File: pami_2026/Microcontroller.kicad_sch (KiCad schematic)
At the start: 20 parts, among them SW1 SW_Reed, U1 ESP32-WROOM-E

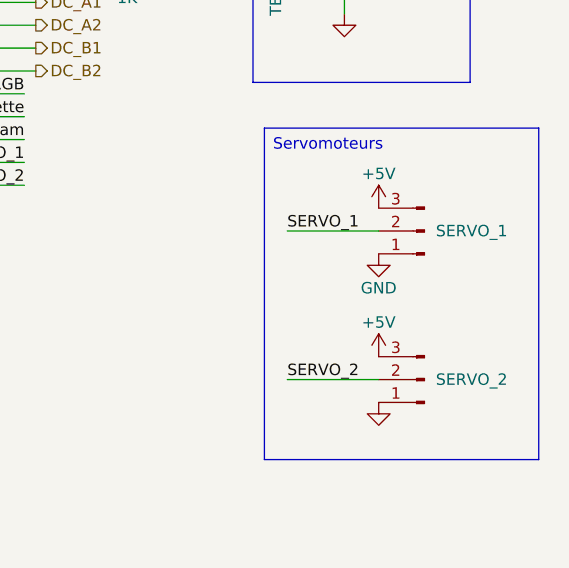
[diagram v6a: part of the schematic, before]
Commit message: Fix servo pinout
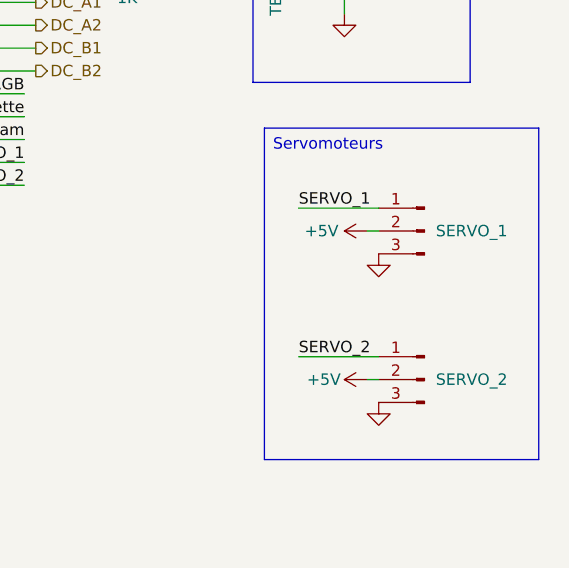
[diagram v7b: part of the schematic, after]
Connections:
- net +5V: now also SERVO_1.2 (Pin_2), SERVO_2.2 (Pin_2); no longer SERVO_1.3 (Pin_3), SERVO_2.3 (Pin_3)
- net GND: now also SERVO_1.3 (Pin_3), SERVO_2.3 (Pin_3); no longer SERVO_1.1 (Pin_1), SERVO_2.1 (Pin_1)
- net SERVO_1: now also SERVO_1.1 (Pin_1); no longer SERVO_1.2 (Pin_2)
- net SERVO_2: now also SERVO_2.1 (Pin_1); no longer SERVO_2.2 (Pin_2)
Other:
- moved on the sheet: SERVO_1, SERVO_2
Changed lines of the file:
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@@
 	(wire
 		(pts
-			(xy 71.12 152.4) (xy 81.28 152.4)
+			(xy 223.52 146.05) (xy 232.41 146.05)
 		)
 		(stroke
@@
 	(wire
 		(pts
-			(xy 97.79 82.55) (xy 97.79 81.28)
+			(xy 71.12 152.4) (xy 81.28 152.4)
 		)
 		(stroke
@@
 	(wire
 		(pts
-			(xy 97.79 90.17) (xy 97.79 91.44)
+			(xy 97.79 82.55) (xy 97.79 81.28)
 		)
 		(stroke
@@
 	(wire
 		(pts
-			(xy 97.79 81.28) (xy 101.6 81.28)
+			(xy 97.79 90.17) (xy 97.79 91.44)
 		)
 		(stroke
@@
 	(wire
 		(pts
-			(xy 87.63 72.39) (xy 87.63 71.12)
+			(xy 97.79 81.28) (xy 101.6 81.28)
 		)
 		(stroke
@@
 	(wire
 		(pts
-			(xy 222.25 148.59) (xy 232.41 148.59)
+			(xy 87.63 72.39) (xy 87.63 71.12)
 		)
 		(stroke
@@
 	(wire
 		(pts
-			(xy 222.25 132.08) (xy 232.41 132.08)
+			(xy 101.6 80.01) (xy 101.6 81.28)
 		)
 		(stroke
@@
 	(wire
 		(pts
-			(xy 101.6 80.01) (xy 101.6 81.28)
+			(xy 193.04 124.46) (xy 181.61 124.46)
 		)
 		(stroke
@@
 	(wire
 		(pts
-			(xy 193.04 124.46) (xy 181.61 124.46)
+			(xy 219.71 67.31) (xy 227.33 67.31)
 		)
 		(stroke
@@
 	(wire
 		(pts
-			(xy 219.71 67.31) (xy 227.33 67.31)
+			(xy 73.66 116.84) (xy 85.09 116.84)
 		)
 		(stroke
@@
 	(wire
 		(pts
-			(xy 73.66 116.84) (xy 85.09 116.84)
+			(xy 191.77 88.9) (xy 181.61 88.9)
 		)
 		(stroke
@@
 	(wire
 		(pts
-			(xy 191.77 88.9) (xy 181.61 88.9)
+			(xy 231.14 148.59) (xy 232.41 148.59)
 		)
 		(stroke
@@
 	(wire
 		(pts
+			(xy 223.52 129.54) (xy 232.41 129.54)
+		)
+		(stroke
+			(width 0)
+			(type default)
+		)
+	)
+	(wire
+		(pts
 			(xy 194.31 114.3) (xy 181.61 114.3)
 		)
@@
 	(wire
 		(pts
+			(xy 231.14 132.08) (xy 232.41 132.08)
+		)
+		(stroke
+			(width 0)
+			(type default)
+		)
+	)
+	(wire
+		(pts
 			(xy 181.61 109.22) (xy 194.31 109.22)
 		)
@@
 	)
 	(label "SERVO_1"
-		(at 222.25 132.08 0)
+		(at 223.52 129.54 0)
 		(effects
 			(font
@@
 	)
 	(label "SERVO_2"
-		(at 222.25 148.59 0)
+		(at 223.52 146.05 0)
 		(effects
 			(font
@@
 	(symbol
 		(lib_id "PCM_SparkFun-PowerSymbol:VCC")
-		(at 232.41 129.54 0)
+		(at 231.14 132.08 90)
 		(unit 1)
 		(exclude_from_sim no)
@@
 		(on_board yes)
 		(dnp no)
-		(fields_autoplaced yes)
 		(property "Reference" "#PWR028"
-			(at 232.41 133.35 0)
+			(at 234.95 132.08 0)
 			(effects
 				(font
@@
 		)
 		(property "Value" "+5V"
-			(at 232.41 125.73 0)
+			(at 226.06 132.08 90)
 			(do_not_autoplace yes)
 			(effects
@@
 		)
 		(property "Footprint" ""
-			(at 232.41 129.54 0)
+			(at 231.14 132.08 0)
 			(effects
 				(font
@@
 		)
 		(property "Datasheet" ""
-			(at 232.41 129.54 0)
+			(at 231.14 132.08 0)
 			(effects
 				(font
@@
 		)
 		(property "Description" "Power symbol creates a global label with name \"VCC\""
-			(at 232.41 135.89 0)
+			(at 237.49 132.08 0)
 			(effects
 				(font
@@
 	(symbol
 		(lib_id "PCM_SparkFun-PowerSymbol:VCC")
-		(at 232.41 146.05 0)
+		(at 231.14 148.59 90)
 		(unit 1)
 		(exclude_from_sim no)
@@
 		(on_board yes)
 		(dnp no)
-		(fields_autoplaced yes)
 		(property "Reference" "#PWR029"
-			(at 232.41 149.86 0)
+			(at 234.95 148.59 0)
 			(effects
 				(font
@@
 		)
 		(property "Value" "+5V"
-			(at 232.41 142.24 0)
+			(at 226.314 148.59 90)
 			(do_not_autoplace yes)
 			(effects
@@
 		)
 		(property "Footprint" ""
-			(at 232.41 146.05 0)
+			(at 231.14 148.59 0)
 			(effects
 				(font
@@
 		)
 		(property "Datasheet" ""
-			(at 232.41 146.05 0)
+			(at 231.14 148.59 0)
 			(effects
 				(font
@@
 		)
 		(property "Description" "Power symbol creates a global label with name \"VCC\""
-			(at 232.41 152.4 0)
+			(at 237.49 148.59 0)
 			(effects
 				(font
@@
 	(symbol
 		(lib_id "Connector:Conn_01x03_Pin")
-		(at 237.49 148.59 180)
+		(at 237.49 148.59 0)
+		(mirror y)
 		(unit 1)
 		(exclude_from_sim no)
@@
 		(on_board yes)
 		(dnp no)
-		(fields_autoplaced yes)
 		(property "Reference" "SERVO_2"
-			(at 238.76 148.5899 0)
+			(at 238.76 148.5901 0)
 			(effects
 				(font
@@
 		)
 		(property "Value" "Conn_01x03_Pin"
-			(at 238.76 149.8599 0)
+			(at 238.76 147.3201 0)
 			(effects
 				(font
@@
 	(symbol
 		(lib_id "Connector:Conn_01x03_Pin")
-		(at 237.49 132.08 180)
+		(at 237.49 132.08 0)
+		(mirror y)
 		(unit 1)
 		(exclude_from_sim no)
@@
 		(on_board yes)
 		(dnp no)
-		(fields_autoplaced yes)
 		(property "Reference" "SERVO_1"
-			(at 238.76 132.0799 0)
+			(at 238.76 132.0801 0)
 			(effects
 				(font
@@
 		)
 		(property "Value" "Conn_01x03_Pin"
-			(at 238.76 133.3499 0)
+			(at 238.76 130.8101 0)
 			(effects
 				(font
@@
 					(size 1.27 1.27)
 				)
+				(hide yes)
 			)
 		)
